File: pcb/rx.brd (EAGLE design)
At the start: 19 x 36 mm, 30 parts, among them J1 USB_A_PTH_MALE, Y1 CRYSTAL-26MHZSMD-3.2X2.5

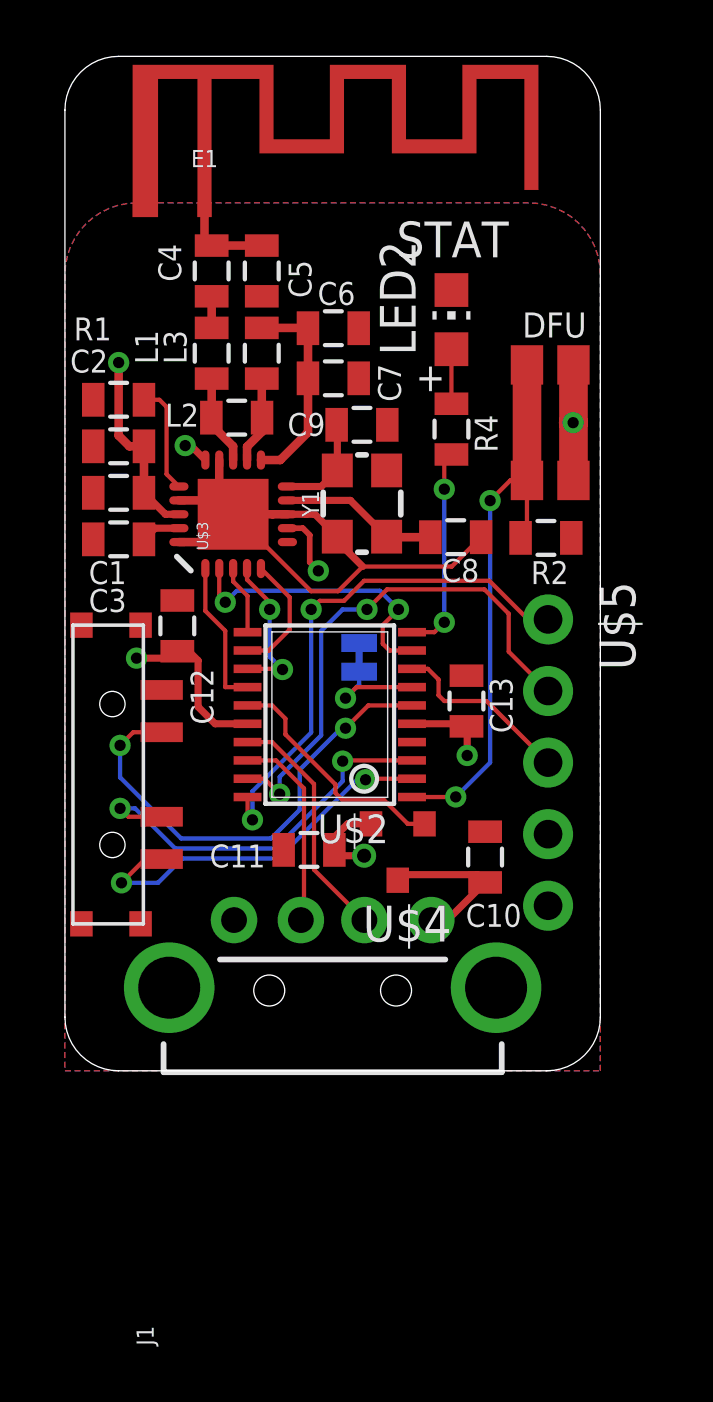
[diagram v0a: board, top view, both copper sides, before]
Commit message: fix silkscreen error, added pogo board
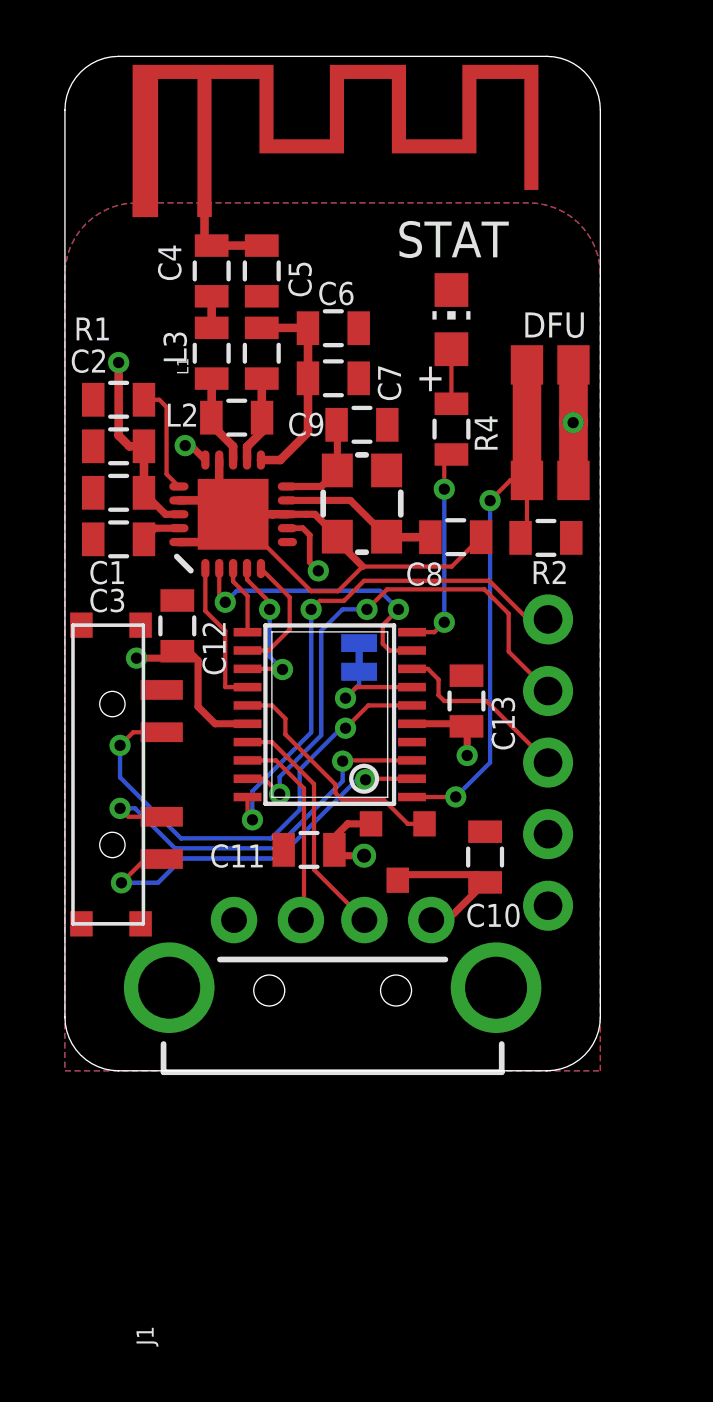
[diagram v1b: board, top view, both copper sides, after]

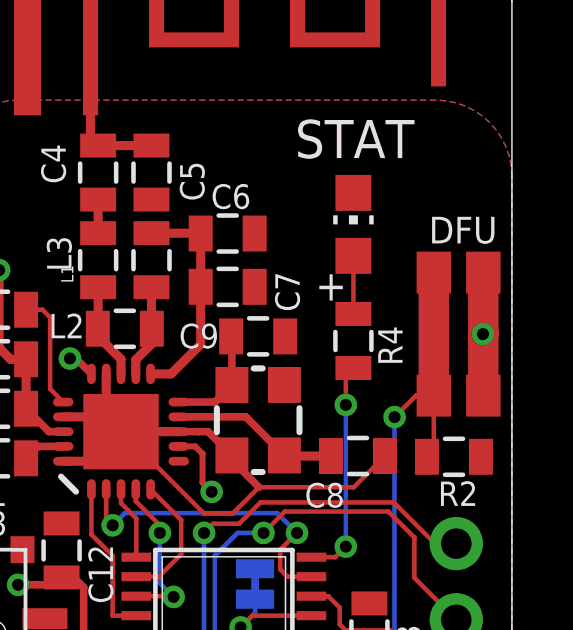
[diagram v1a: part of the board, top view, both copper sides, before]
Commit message: added holes to button
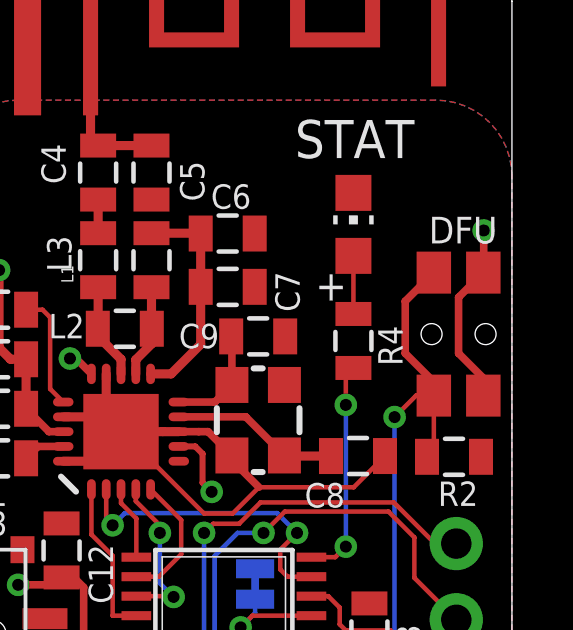
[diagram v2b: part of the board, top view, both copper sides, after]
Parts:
- U$10: value 324_SW -> 324_SW324_SWITCH_FOOT_HOLE; device 3pos_slide_switch:342_SWICH_FOOT -> 3pos_slide_switch:342_SWICH_FOOT_HOLE
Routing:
- net +3V3: track 26.4 -> 28.4 mm
- net N$11: track 20.4 -> 21.2 mm
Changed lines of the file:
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@@
 </element>
 <element name="SJ1" library="SparkFun-Jumpers" package="SMT-JUMPER_2_NC_TRACE_NO-SILK" value="JUMPER-SMT_2_NC_TRACE_NO-SILK" x="10.4394" y="14.6718" smashed="yes" rot="MR270"/>
-<element name="U$10" library="3pos_slide_switch" package="342_SWICH_FOOT" value="324_SW" x="17.2212" y="23.0002" smashed="yes" rot="R90"/>
+<element name="U$10" library="3pos_slide_switch" package="342_SWICH_FOOT_HOLE" value="324_SW324_SWITCH_FOOT_HOLE" x="17.2212" y="23.0002" smashed="yes" rot="R90"/>
 <element name="LED2" library="joyAnalog" package="CHIP-LED0805" value="" x="13.716" y="26.6578" smashed="yes">
 <attribute name="VALUE" x="16.256" y="25.3878" size="1.27" layer="27" rot="R90"/>
@@
 <contactref element="SJ1" pad="1"/>
 <contactref element="U$10" pad="P$4"/>
-<via x="18.034" y="23.0002" extent="1-16" drill="0.4"/>
+<via x="18.0594" y="26.4546" extent="1-16" drill="0.4"/>
 <wire x1="8.4433" y1="19.2559" x2="7.8944" y2="19.2559" width="0.2032" layer="1"/>
 <wire x1="8.6868" y1="19.0124" x2="8.4433" y2="19.2559" width="0.2032" layer="1"/>
 <contactref element="U$10" pad="P$1"/>
-<wire x1="18.0462" y1="25.0502" x2="18.0462" y2="23.0124" width="1.016" layer="1"/>
-<wire x1="18.0462" y1="23.0124" x2="18.034" y2="23.0002" width="1.016" layer="1"/>
-<wire x1="18.0462" y1="20.9502" x2="18.0462" y2="23.0124" width="1.016" layer="1"/>
 <contactref element="U$2" pad="16"/>
 <contactref element="U$2" pad="5"/>
@@
 <wire x1="8.9916" y1="17.7424" x2="8.6868" y2="18.0472" width="0.2032" layer="1"/>
 <wire x1="8.6868" y1="18.0472" x2="8.6868" y2="19.0124" width="0.2032" layer="1"/>
+<wire x1="18.0594" y1="26.4546" x2="18.0594" y2="25.0634" width="0.254" layer="1"/>
+<wire x1="18.0594" y1="25.0634" x2="18.0462" y2="25.0502" width="0.254" layer="1"/>
+<wire x1="18.0462" y1="25.0502" x2="17.2212" y2="24.2252" width="0.254" layer="1"/>
+<wire x1="17.2212" y1="22.3594" x2="18.0462" y2="21.5344" width="0.254" layer="1"/>
+<wire x1="17.2212" y1="24.2252" x2="17.2212" y2="22.3594" width="0.254" layer="1"/>
+<wire x1="18.0462" y1="21.5344" x2="18.0462" y2="20.9502" width="0.254" layer="1"/>
 </signal>
 <signal name="N$1">
@@
 <contactref element="U$10" pad="P$2"/>
 <contactref element="U$10" pad="P$3"/>
-<wire x1="16.3962" y1="25.0502" x2="16.3962" y2="20.9502" width="1.016" layer="1"/>
 <contactref element="U$2" pad="1"/>
 <wire x1="12.3158" y1="9.7148" x2="13.8644" y2="9.7148" width="0.1524" layer="1"/>
@@
 <wire x1="15.0876" y1="10.938" x2="15.0876" y2="20.2344" width="0.1524" layer="16"/>
 <wire x1="13.8684" y1="9.7188" x2="13.8644" y2="9.7148" width="0.1524" layer="1"/>
+<wire x1="16.3962" y1="25.0502" x2="15.4432" y2="24.0972" width="0.254" layer="1"/>
+<wire x1="15.4432" y1="22.3604" x2="16.3962" y2="21.4074" width="0.254" layer="1"/>
+<wire x1="15.4432" y1="24.0972" x2="15.4432" y2="22.3604" width="0.254" layer="1"/>
+<wire x1="16.3962" y1="21.4074" x2="16.3962" y2="20.9502" width="0.254" layer="1"/>
 </signal>
 <signal name="N$12">

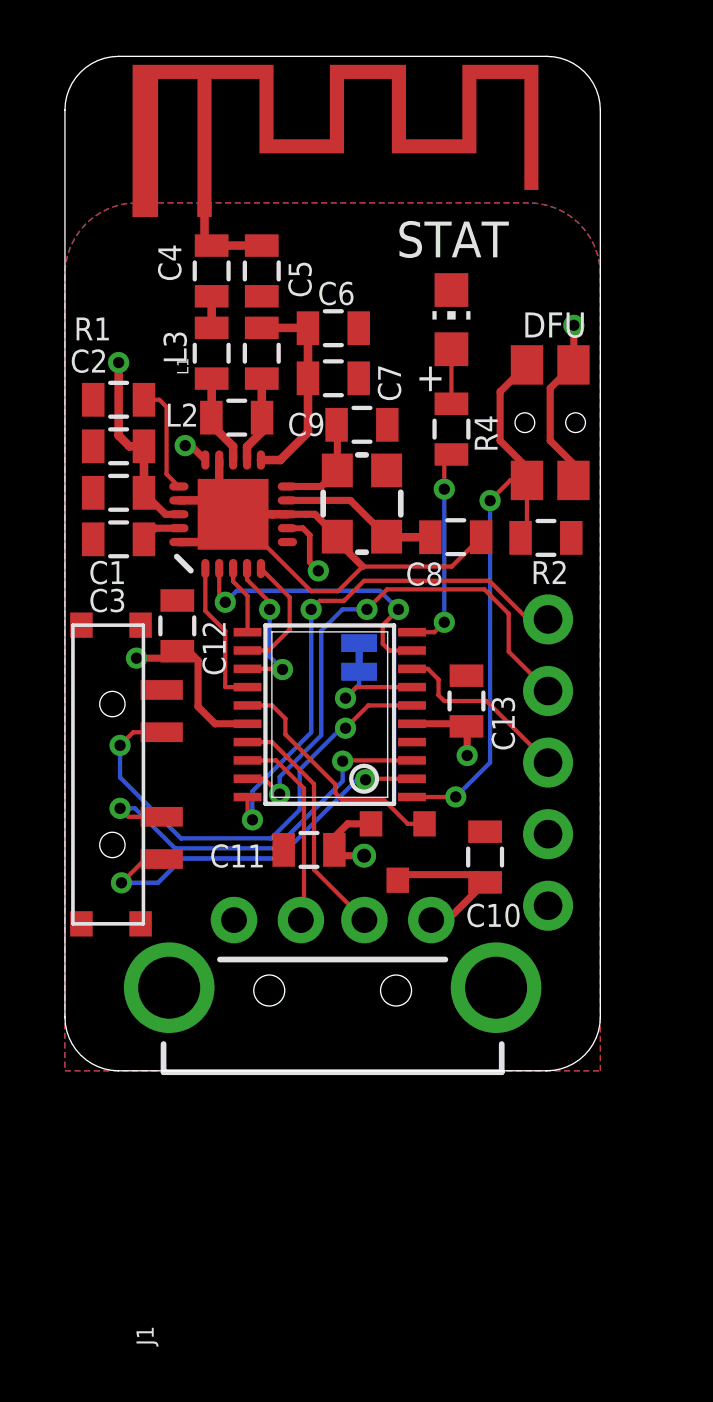
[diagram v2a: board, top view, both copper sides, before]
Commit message: updated PCB, firmware sleep working
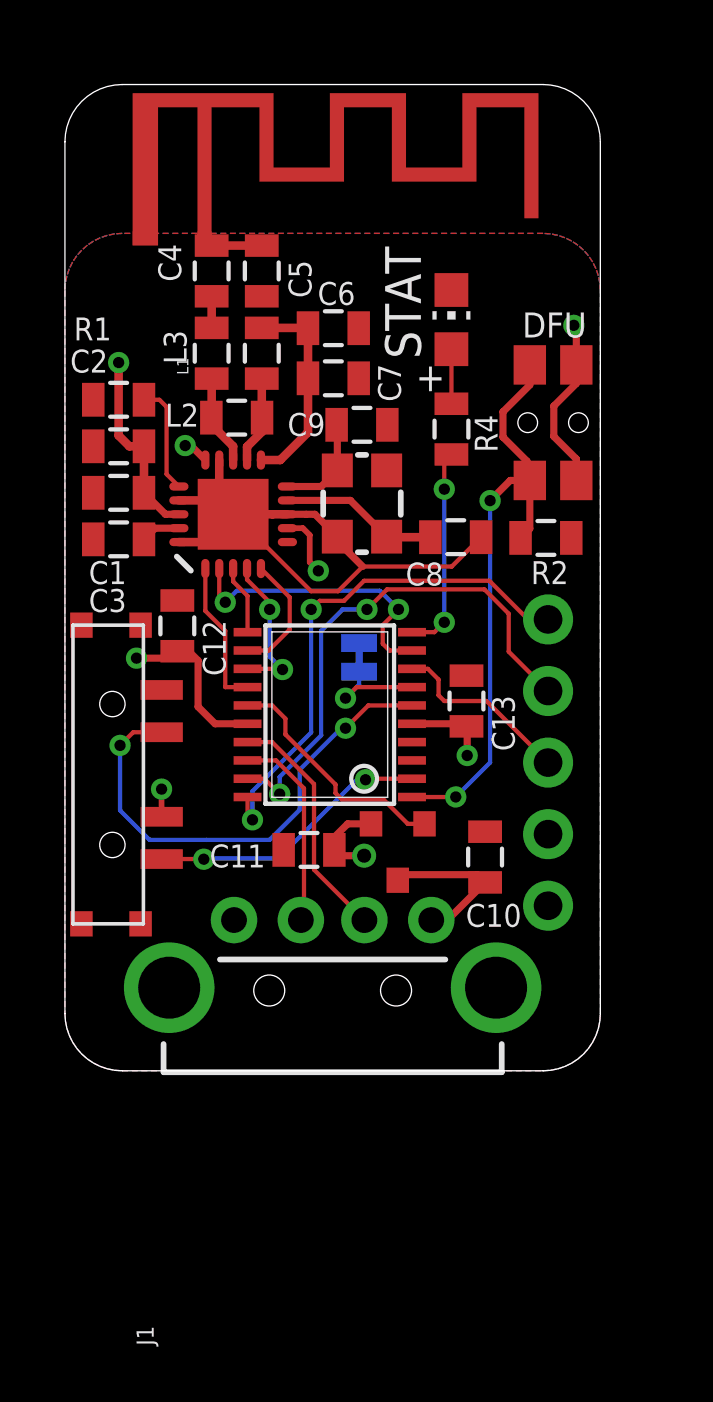
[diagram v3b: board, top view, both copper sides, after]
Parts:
- moved E1 1.00 mm to (4.95, 29.8)
- moved U$10 0.10 mm to (17.3, 23.0)
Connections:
- removed net N$25: U$1.P$7, U$2.3
- net +3V3: now also U$1.P$7
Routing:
- net N$25: track 14.3 -> 0.00 mm, vias 2 -> 0
- net N$10: track 13.6 -> 10.1 mm
- net N$5: track 3.15 -> 2.14 mm
- net +3V3: track 28.4 -> 29.4 mm, vias 7 -> 8
- net N$26: track 16.9 -> 17.6 mm
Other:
- board size 19 x 36 mm -> 19 x 35 mm
